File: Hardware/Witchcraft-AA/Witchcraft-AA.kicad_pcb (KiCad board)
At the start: 2 copper layers, 180 x 81 mm, 48 parts, among them J0 USB_C_Molex_201267-0005, J1 USB_C_Molex_201267-0005, J3 Conn_01x05_Socket, J4 Conn_NREC007, J6 10157930, J7 Amphenol_101019966912A, U1 Z1 extreme, U2 LM26420-Q1xx-xxxx, U3 K3LKCKC0BM, U4 K3LKCKC0BM

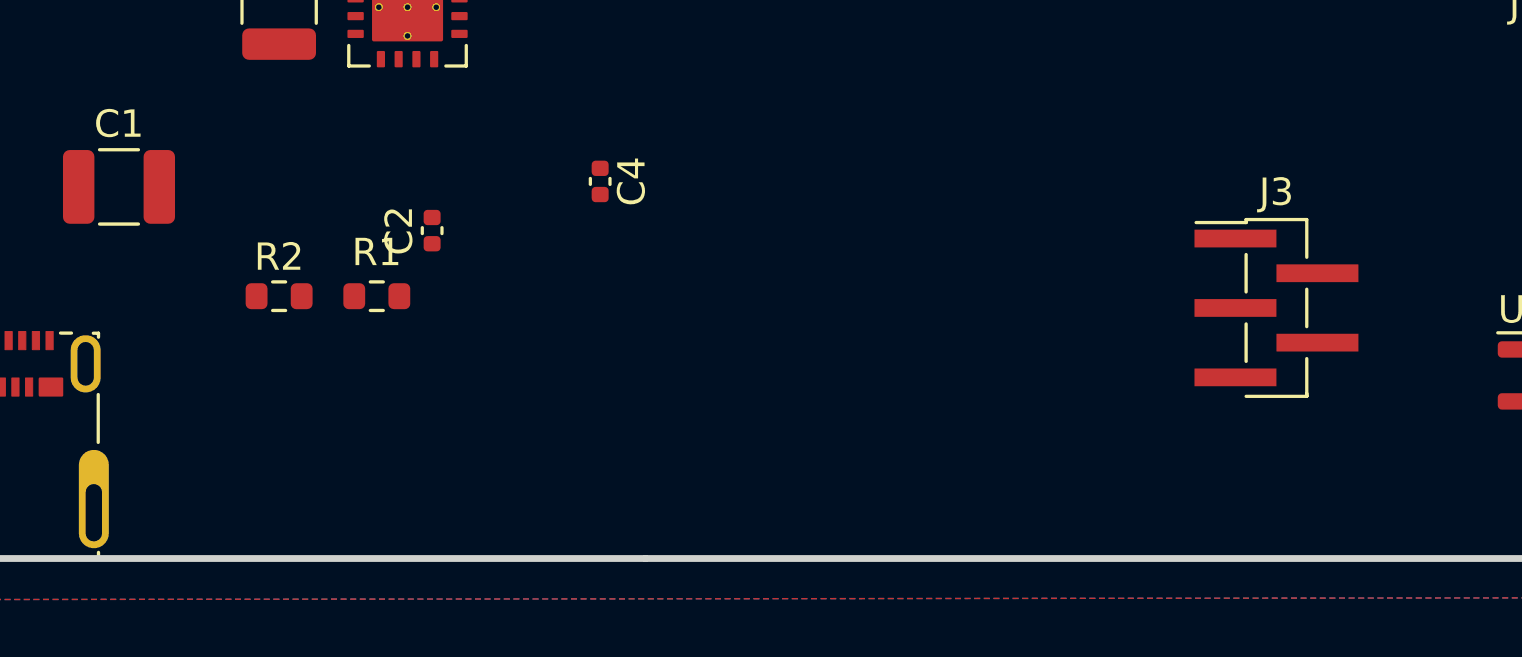
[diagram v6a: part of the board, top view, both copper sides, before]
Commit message: ECAD: replaced the Z1 Extreme with the 7840U chip, as the AI-engine will be more useful for makers and non-gamers. MCAD: continued converting the outer shell towards a Assembly4-architecture, adding more items. Started a big change in design wherein I'm splitting the shell-design into a modular one, to accomodate removable controllers. Made some minor tweaks to the cooling-assembly, to accomodate the new, split shell-design. Updated the Readme to describe the project.
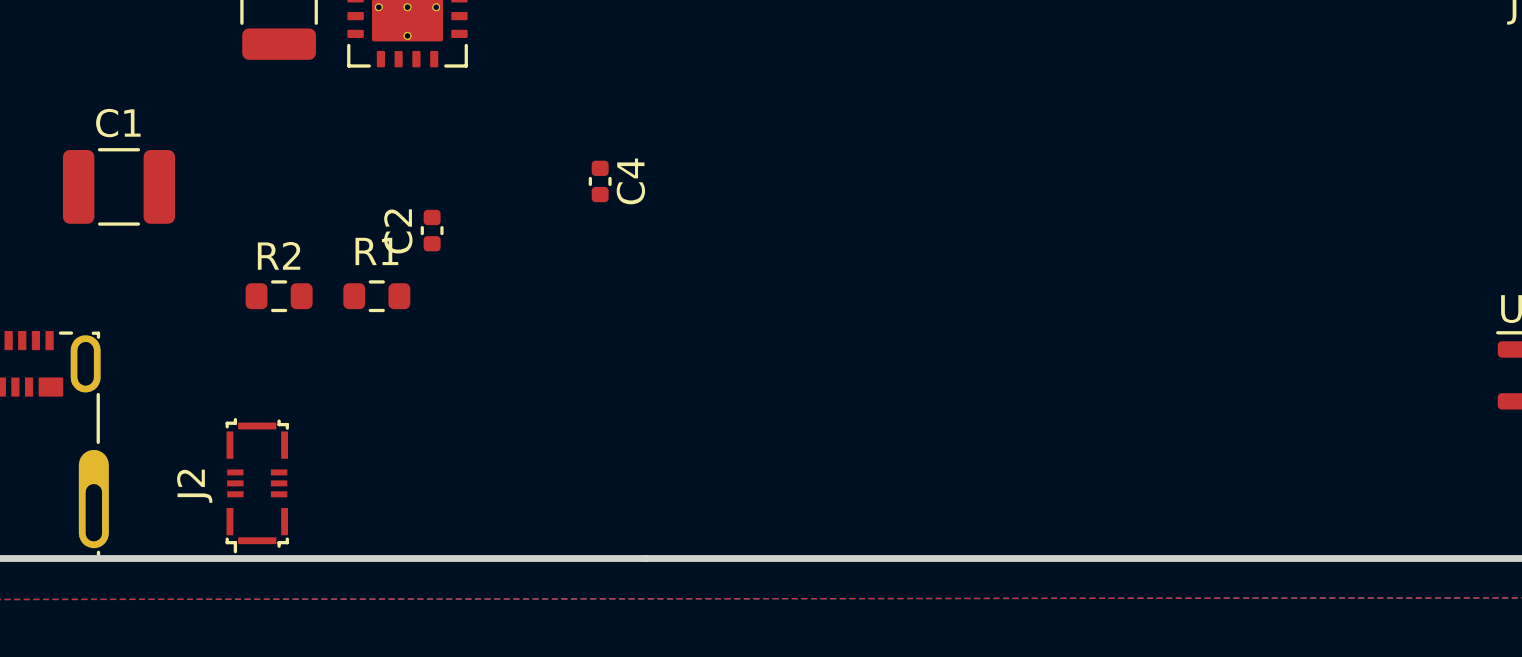
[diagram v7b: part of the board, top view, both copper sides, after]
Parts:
- removed J3: Conn_01x05_Socket, Connector_PinHeader_1.27mm:PinHeader_1x05_P1.27mm_Vertical_SMD_Pin1Left
- added J2: ~, LRJ:Samsung_Hirose_xxx-xxx_2x3_P0.35mm_Vertical, F.Cu at (10.8, 37.8)

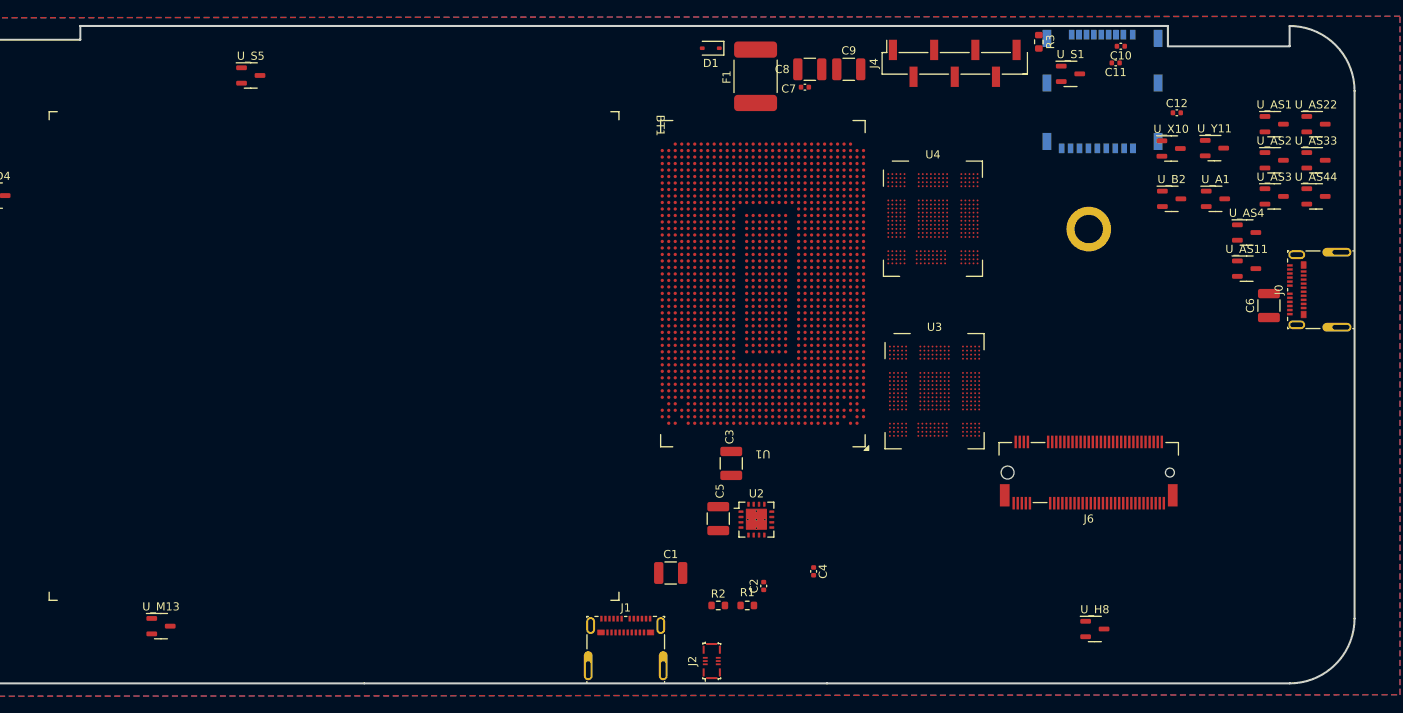
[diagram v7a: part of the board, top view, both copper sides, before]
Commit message: MCAD: Added Oculink connector. ECAD: Added Oculink connector.
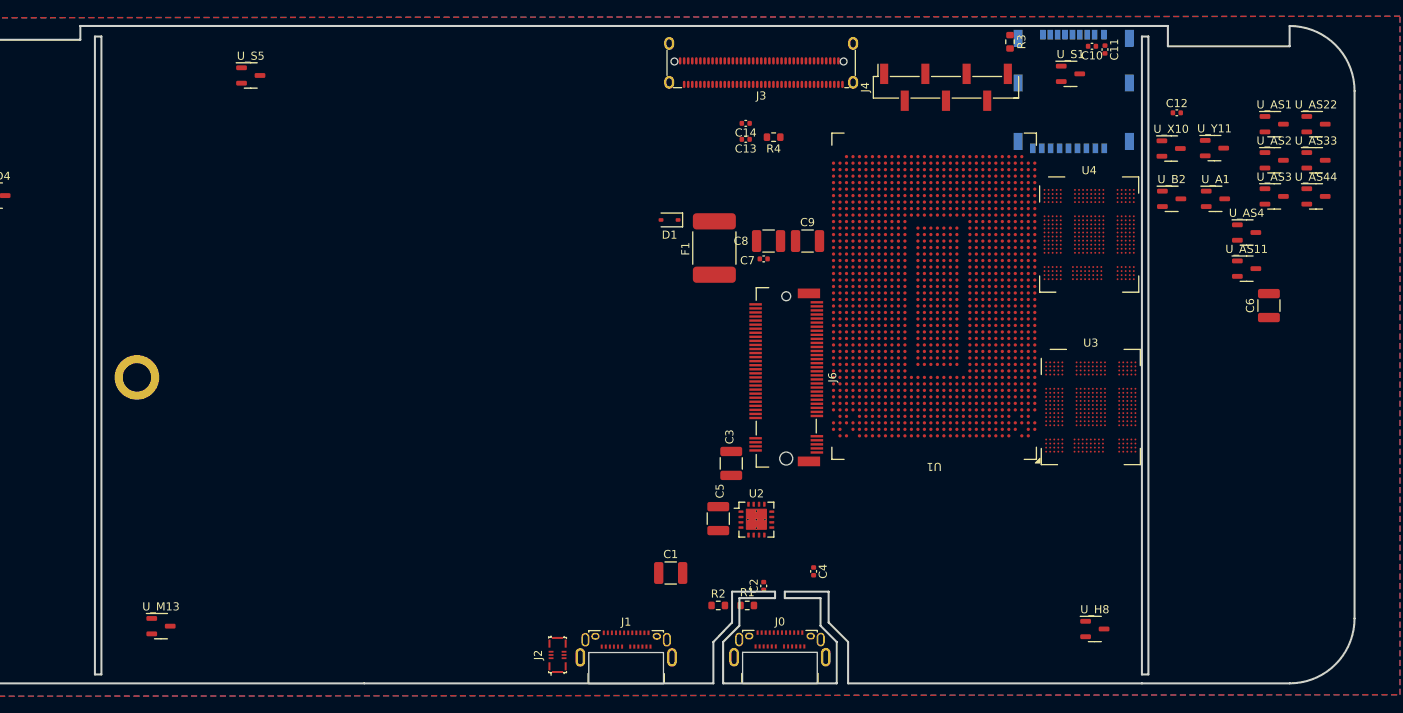
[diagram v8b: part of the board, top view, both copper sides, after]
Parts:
- added C13: C_CGA2B1X7R1V224K, Capacitor_SMD:C_0402_1005Metric, F.Cu at (15.0, -26.5)
- added C14: C_CGA2B1X7R1V224K, Capacitor_SMD:C_0402_1005Metric, F.Cu at (15.0, -28.5)
- added J3: OCuLink_8i, LRJ:Molex_Nano-Pitch_173162-xx32_2x40_P0.50mm_Horizontal, F.Cu at (16.9, -37.5)
- added R4: R_ERJ-3GEYJ105V, Resistor_SMD:R_0603_1608Metric, F.Cu at (18.4, -26.8)
- BT1: moved to B.Cu
- J0, J1: value USB_C_Molex_201267-0005 -> USB_C_Amphenol_12402136E512A; footprint LRJ:USB-C_Receptacle_2012670005 -> LRJ:USB-C_Receptacle_Amphenol_12402136E512A
- J6: footprint LRJ:Amphenol_10157930_PCI_Express_M.2_2230_less-court -> LRJ:Amphenol_10157930_PCI_Express_M.2_2280_less-court
- U1: value Z1 extreme -> AMD Ryzen 7840U
- moved J0 81.3 mm to (19.2, 38.4), turned to 0 degrees
- moved J6 39.1 mm to (20.0, 2.80), turned to 90 degrees
- moved F1 21.8 mm to (11.1, -13.0)
- moved C7 21.8 mm to (17.2, -11.8)
- moved C8 21.8 mm to (17.8, -14.0)
- moved C9 21.8 mm to (22.6, -14.0)
- moved D1 21.8 mm to (5.60, -16.6)
- moved U1 21.2 mm to (38.2, -7.20)
- moved U3 19.3 mm to (57.5, 6.45)
- moved U4 19.3 mm to (57.3, -14.8)
- moved J2 19.0 mm to (-8.20, 37.0)
- moved BT1 10.0 mm to (-27.4, -5.40), turned to 0 degrees
- moved C10 3.55 mm to (57.6, -38.0)
- moved J7 3.55 mm to (55.4, -32.6)
- moved R3 3.55 mm to (47.5, -38.5)
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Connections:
- U1 pad A11: (no net) -> unconnected-(U1C-~{MAB1_CLK_0}-PadA11)
- U1 pad A14: GND -> (no net)
- U1 pad A19: GND -> unconnected-(U1G-PCIE_RX1+-PadA19)
- U1 pad A21: GND -> unconnected-(U1G-PCIE_RX3+-PadA21)
- U1 pad A22: unconnected-(U1G-PCIE_RX4+-PadA22) -> (no net)
- U1 pad A23: GND -> unconnected-(U1G-PCIE_RX5+-PadA23)
- U1 pad A27: unconnected-(U1G-PCIE_RX9+-PadA27) -> /PCIe/PCIE_RX9+
- U1 pad A28: unconnected-(U1G-PCIE_RX10+-PadA28) -> /PCIe/PCIE_RX10+
- U1 pad A3: GND -> (no net)
- U1 pad A31: unconnected-(U1G-PCIE_RX13+-PadA31) -> /PCIe/PCIE_RX13+
- U1 pad B26: unconnected-(U1G-PCIE_RX8--PadB26) -> /PCIe/PCIE_RX8-
- U1 pad B27: unconnected-(U1G-PCIE_RX9--PadB27) -> /PCIe/PCIE_RX9-
- U1 pad B29: unconnected-(U1G-PCIE_RX11--PadB29) -> /PCIe/PCIE_RX11-
- U1 pad B31: unconnected-(U1G-PCIE_RX13--PadB31) -> /PCIe/PCIE_RX13-
- U1 pad B32: unconnected-(U1G-PCIE_RX14--PadB32) -> /PCIe/PCIE_RX14-
- U1 pad C26: unconnected-(U1G-PCIe_TX8+-PadC26) -> /PCIe/PCIE_TX8+
- U1 pad C27: unconnected-(U1G-PCIe_TX9+-PadC27) -> /PCIe/PCIE_TX9+
- U1 pad C28: unconnected-(U1G-PCIe_TX10+-PadC28) -> /PCIe/PCIE_TX10+
- U1 pad C29: unconnected-(U1G-PCIe_TX11+-PadC29) -> /PCIe/PCIE_TX11+
- U1 pad C30: unconnected-(U1G-PCIe_TX12+-PadC30) -> /PCIe/PCIE_TX12+
- U1 pad C31: unconnected-(U1G-PCIe_TX13+-PadC31) -> /PCIe/PCIE_TX13+
- U1 pad C32: GND -> /PCIe/PCIE_TX14+
- U1 pad D14: (no net) -> GND
- U1 pad D26: unconnected-(U1G-PCIe_TX8--PadD26) -> /PCIe/PCIE_TX8-
- U1 pad D27: unconnected-(U1G-PCIe_TX9--PadD27) -> /PCIe/PCIE_TX9-
- U1 pad D28: unconnected-(U1G-PCIe_TX10--PadD28) -> /PCIe/PCIE_TX10-
- U1 pad D30: unconnected-(U1G-PCIe_TX12--PadD30) -> /PCIe/PCIE_TX12-
- U1 pad D31: unconnected-(U1G-PCIe_TX13--PadD31) -> /PCIe/PCIE_TX13-
- U1 pad E32: (no net) -> GND
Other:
- outline, holes or cut-outs redrawn
